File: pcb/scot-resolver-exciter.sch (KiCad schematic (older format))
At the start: 27 parts, among them IC1 AD8692ARMZ, IC2 AD8397ARZ

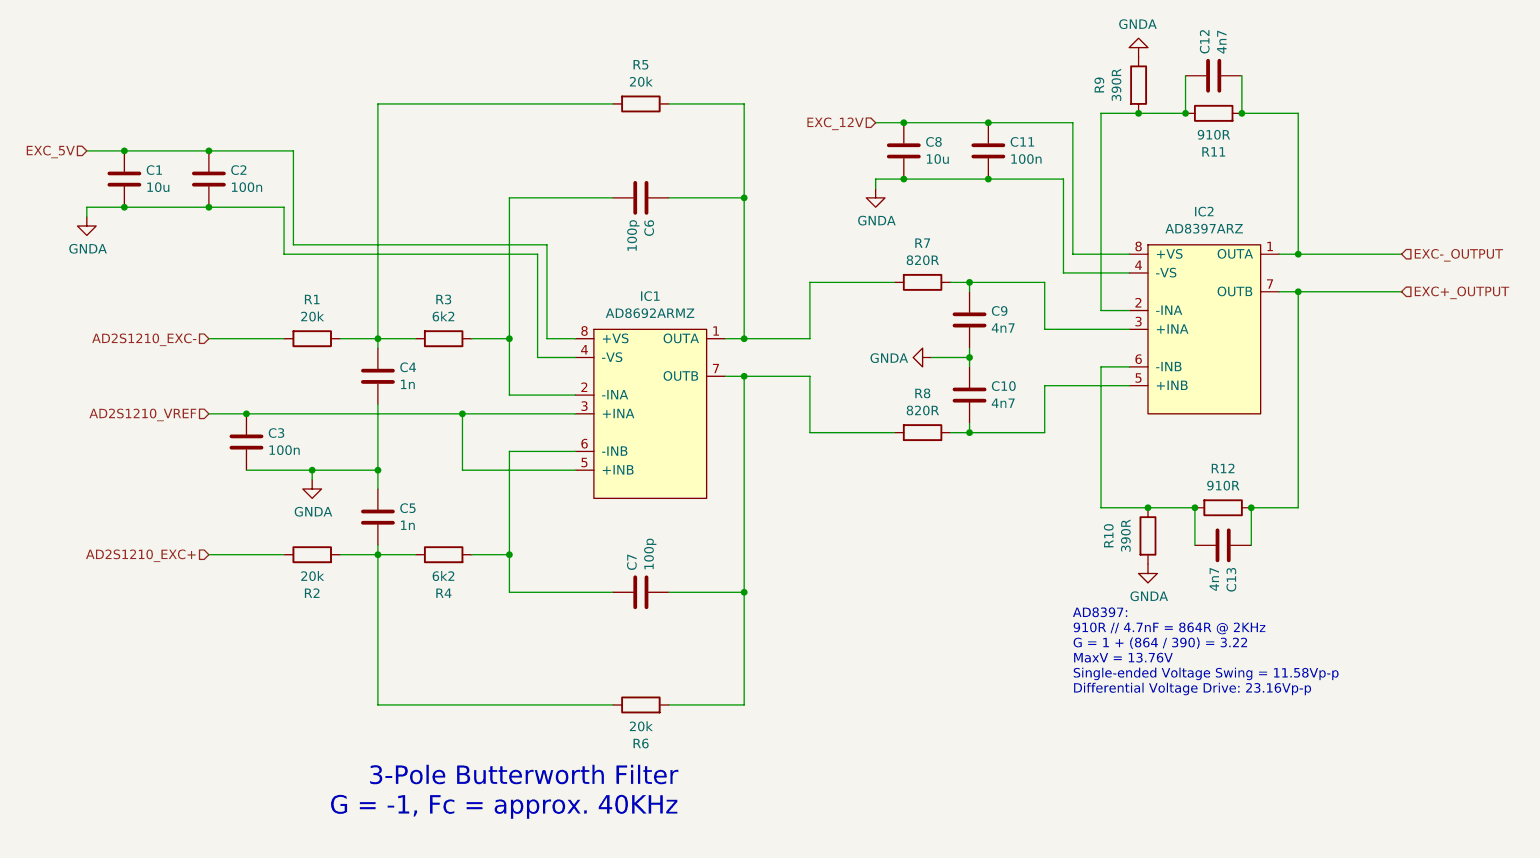
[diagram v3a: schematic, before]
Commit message: pcb: Clear up exciter ground rail (sch & pcb).
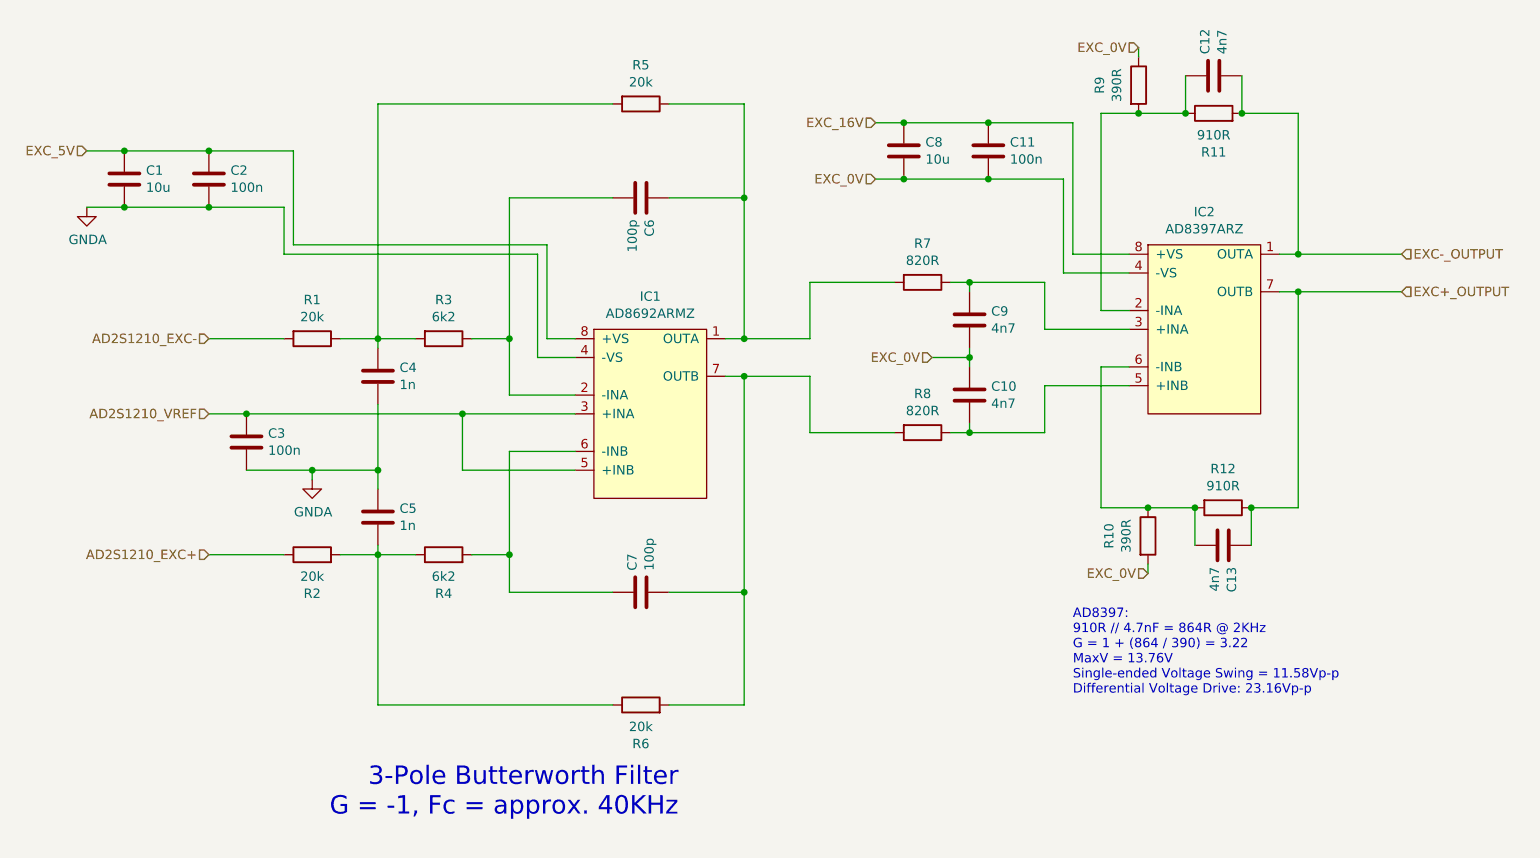
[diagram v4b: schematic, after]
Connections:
- net GNDA: no longer C10.1, C11.2, C8.2, C9.2, IC2.4 (-VS), R10.2, R9.1
- net EXC_12V renamed EXC_16V
- new net EXC_0V: C10.1, C11.2, C8.2, C9.2, IC2.4 (-VS), R10.2, R9.1
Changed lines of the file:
@@
 $EndComp
 Text HLabel 7250 2200 0    50   Input ~ 0
-EXC_12V
+EXC_16V
 Wire Wire Line
 	7400 2200 7850 2200
-Wire Wire Line
-	7250 2550 7250 2500
 Wire Wire Line
 	7250 2500 7400 2500
@@
 	3250 2350 3700 2350
 Wire Wire Line
-	3050 2700 3050 2650
-Wire Wire Line
 	3050 2650 3250 2650
 Connection ~ 3250 2650
@@
 EXC_5V
 $Comp
-L power:GNDA #PWR0104
-U 1 1 5E286735
-P 3050 2700
-F 0 "#PWR0104" H 3050 2450 50  0001 C CNN
-F 1 "GNDA" H 3055 2527 50  0000 C CNN
-F 2 "" H 3050 2700 50  0001 C CNN
-F 3 "" H 3050 2700 50  0001 C CNN
-	1    3050 2700
-	1    0    0    -1
-$EndComp
-$Comp
-L power:GNDA #PWR0105
-U 1 1 5E288CE0
-P 4250 4100
-F 0 "#PWR0105" H 4250 3850 50  0001 C CNN
-F 1 "GNDA" H 4255 3927 50  0000 C CNN
-F 2 "" H 4250 4100 50  0001 C CNN
-F 3 "" H 4250 4100 50  0001 C CNN
-	1    4250 4100
-	1    0    0    -1
-$EndComp
-$Comp
-L power:GNDA #PWR0106
-U 1 1 5E289B5A
-P 7550 3450
-F 0 "#PWR0106" H 7550 3200 50  0001 C CNN
-F 1 "GNDA" V 7555 3323 50  0000 R CNN
-F 2 "" H 7550 3450 50  0001 C CNN
-F 3 "" H 7550 3450 50  0001 C CNN
-	1    7550 3450
-	0    1    1    0
-$EndComp
-$Comp
-L power:GNDA #PWR0107
-U 1 1 5E28AC14
-P 7250 2550
-F 0 "#PWR0107" H 7250 2300 50  0001 C CNN
-F 1 "GNDA" H 7255 2377 50  0000 C CNN
-F 2 "" H 7250 2550 50  0001 C CNN
-F 3 "" H 7250 2550 50  0001 C CNN
-	1    7250 2550
-	1    0    0    -1
-$EndComp
-$Comp
-L power:GNDA #PWR0108
-U 1 1 5E28B88D
-P 8700 4550
-F 0 "#PWR0108" H 8700 4300 50  0001 C CNN
-F 1 "GNDA" H 8705 4377 50  0000 C CNN
-F 2 "" H 8700 4550 50  0001 C CNN
-F 3 "" H 8700 4550 50  0001 C CNN
-	1    8700 4550
-	1    0    0    -1
-$EndComp
-$Comp
-L power:GNDA #PWR0109
-U 1 1 5E28BEA1
-P 8650 1850
-F 0 "#PWR0109" H 8650 1600 50  0001 C CNN
-F 1 "GNDA" H 8655 1677 50  0000 C CNN
-F 2 "" H 8650 1850 50  0001 C CNN
-F 3 "" H 8650 1850 50  0001 C CNN
-	1    8650 1850
-	-1   0    0    1
-$EndComp
-$Comp
 L Device:C C12
 U 1 1 5E0B3AAD
@@
 Text Notes 8300 5250 0    50   ~ 0
 AD8397:\n910R // 4.7nF = 864R @ 2KHz\nG = 1 + (864 / 390) = 3.22\nMaxV = 13.76V\nSingle-ended Voltage Swing = 11.58Vp-p\nDifferential Voltage Drive: 23.16Vp-p
+Text HLabel 7250 2500 0    50   Input ~ 0
+EXC_0V
+Text HLabel 7550 3450 0    50   Input ~ 0
+EXC_0V
+Text HLabel 8700 4600 0    50   Input ~ 0
+EXC_0V
+Wire Wire Line
+	8700 4600 8700 4550
+Text HLabel 8650 1800 0    50   Input ~ 0
+EXC_0V
+Wire Wire Line
+	8650 1800 8650 1850
+$Comp
+L power:GNDA #PWR?
+U 1 1 5ED769F0
+P 3050 2650
+F 0 "#PWR?" H 3050 2400 50  0001 C CNN
+F 1 "GNDA" H 3055 2477 50  0000 C CNN
+F 2 "" H 3050 2650 50  0001 C CNN
+F 3 "" H 3050 2650 50  0001 C CNN
+	1    3050 2650
+	1    0    0    -1
+$EndComp
+$Comp
+L power:GNDA #PWR?
+U 1 1 5ED77326
+P 4250 4100
+F 0 "#PWR?" H 4250 3850 50  0001 C CNN
+F 1 "GNDA" H 4255 3927 50  0000 C CNN
+F 2 "" H 4250 4100 50  0001 C CNN
+F 3 "" H 4250 4100 50  0001 C CNN
+	1    4250 4100
+	1    0    0    -1
+$EndComp
 $EndSCHEMATC
